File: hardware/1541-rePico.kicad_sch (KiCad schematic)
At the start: 11 parts, among them J1 Display Connector, J2 Conn_02x03_Odd_Even, J3 RESET_1541, J4 SD Card Module Connector, J5 EXT_5V, SW1 RESET, U1 Pico

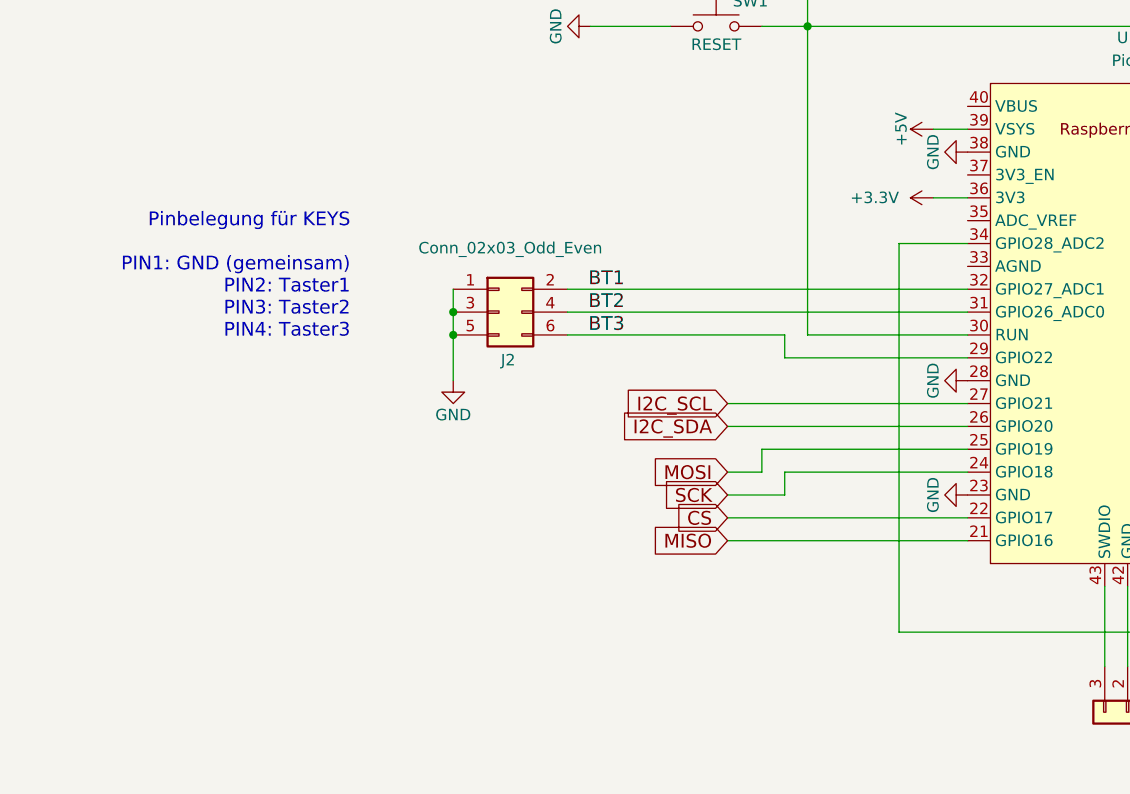
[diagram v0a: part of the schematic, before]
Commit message: new PCB layout + BRDY fix
changed rotary-encoder connector to default 5 pin
flipped BRDY signal (GPIO28) with BT3 (GPIO22) to
 not violate 5V tollerance of GPIO28.
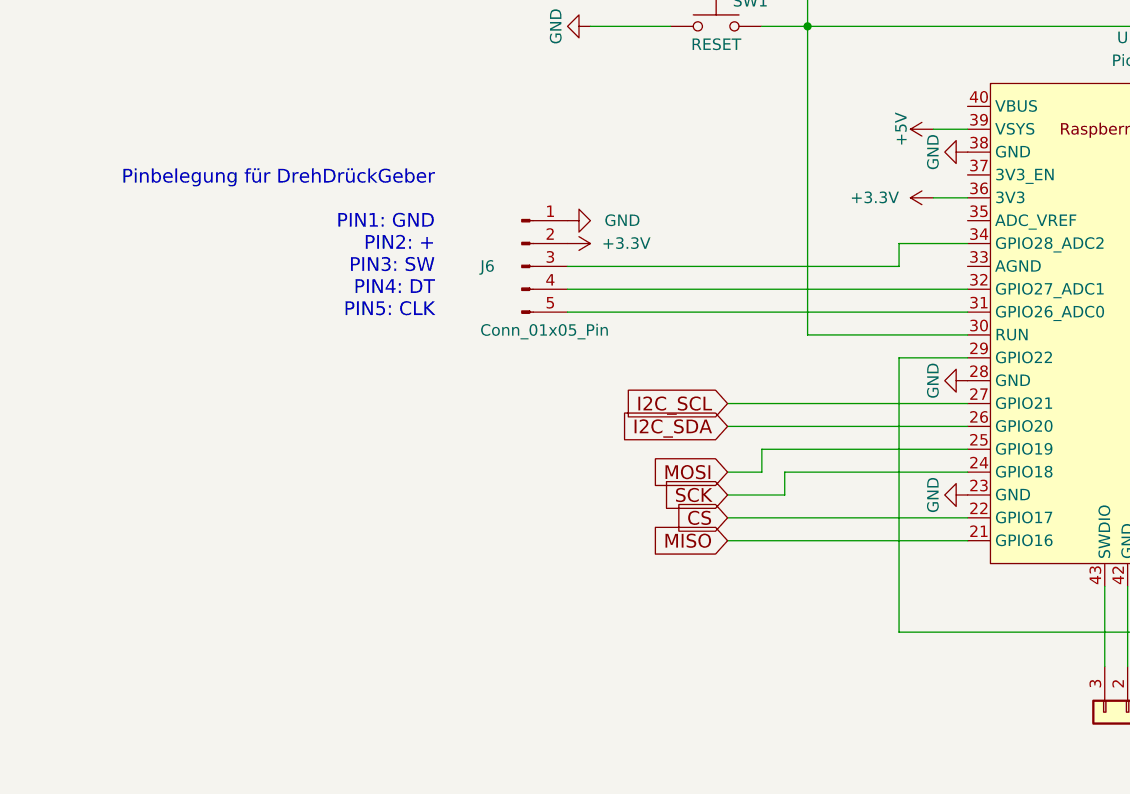
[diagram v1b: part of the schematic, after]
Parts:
- removed J2: Conn_02x03_Odd_Even, Connector_PinHeader_2.54mm:PinHeader_2x03_P2.54mm_Vertical, symbol Connector_Generic:Conn_02x03_Odd_Even
- added J6: Conn_01x05_Pin, Connector_PinHeader_2.54mm:PinHeader_1x05_P2.54mm_Vertical, symbol Connector:Conn_01x05_Pin
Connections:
- net BT3 is gone; now on net VIA 6522 Sockel/BRDY: U1.29 (GPIO22)
- net +3.3V: now also J6.2 (Pin_2)
- net GND: now also J6.1 (Pin_1)
- net VIA 6522 Sockel/BRDY: no longer U1.34 (GPIO28_ADC2)
- net BT1: no longer names the net of U1.32 (GPIO27_ADC1)
- net BT1: now also J6.4 (Pin_4)
- net BT2: no longer names the net of U1.31 (GPIO26_ADC0)
- net BT2: now also J6.5 (Pin_5)
- new net: J6.3 (Pin_3), U1.34 (GPIO28_ADC2)
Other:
- note added: "Pinbelegung für DrehDrückGeber PIN1: GND PIN2: + PIN3: SW PIN4: DT PIN5: CLK"
- note removed: "Pinbelegung für KEYS PIN1: GND (gemeinsam) PIN2: Taster1 PIN3: Taster2 PIN4: Taster3"

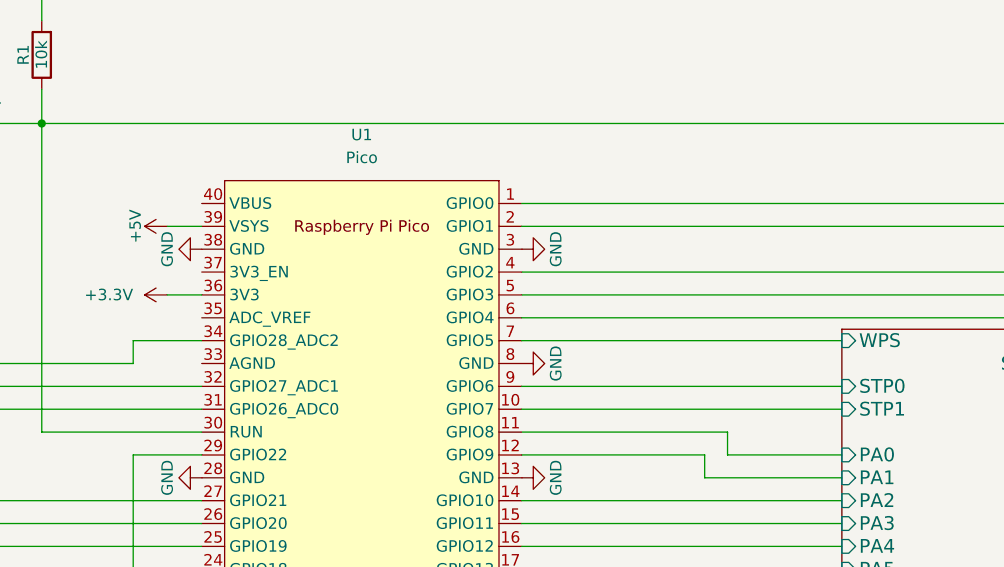
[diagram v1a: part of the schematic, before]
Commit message: new PCB layout to support WPS external
invert WPS signal to be used as input of photo-sensor
circuit of 1541-main pcb.
avoids the concurrent access of the WPS signal between
GateArray and VIA - now this comes from 74LS04
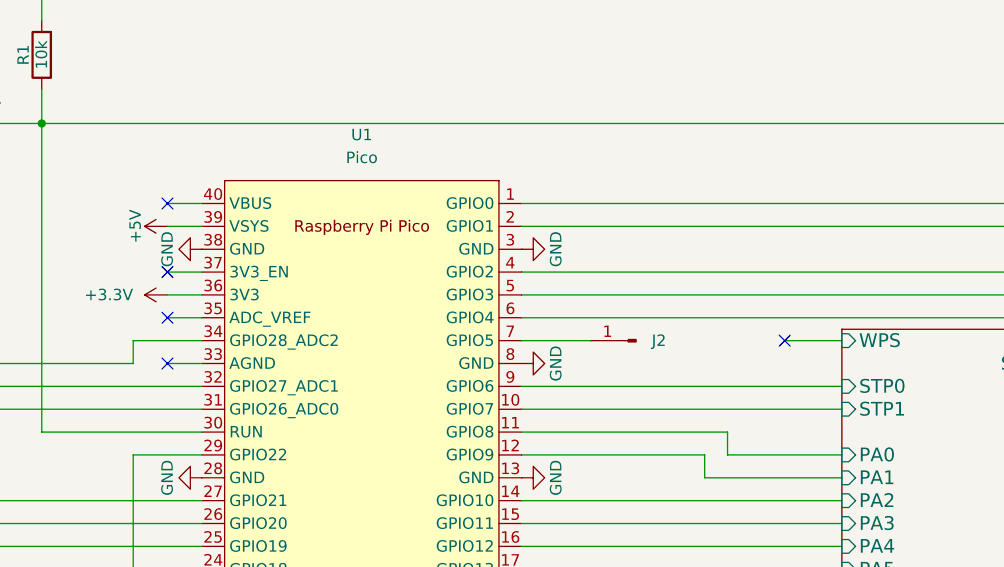
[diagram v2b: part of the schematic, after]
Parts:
- added J2: Conn_01x01_Pin, Connector_PinHeader_2.00mm:PinHeader_1x01_P2.00mm_Vertical, symbol Connector:Conn_01x01_Pin
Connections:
- net VIA 6522 Sockel/WPS: no longer U1.7 (GPIO5)
- new net: J2.1 (Pin_1), U1.7 (GPIO5)
- no-connect marks 0 -> 5
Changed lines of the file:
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@@
 		(title "1541-rePico")
 		(date "2026-02-15")
-		(rev "1.3")
+		(rev "1.4")
 	)
 	(text "Jumper Normal offen"
@@
 		(color 0 0 0 0)
 	)
+	(no_connect
+		(at 116.84 85.09)
+	)
+	(no_connect
+		(at 116.84 80.01)
+	)
+	(no_connect
+		(at 116.84 90.17)
+	)
+	(no_connect
+		(at 116.84 72.39)
+	)
+	(no_connect
+		(at 185.42 87.63)
+	)
 	(wire
 		(pts
@@
 	(wire
 		(pts
+			(xy 116.84 72.39) (xy 120.65 72.39)
+		)
+		(stroke
+			(width 0)
+			(type default)
+		)
+	)
+	(wire
+		(pts
 			(xy 113.03 87.63) (xy 113.03 90.17)
 		)
@@
 	(wire
 		(pts
+			(xy 116.84 90.17) (xy 120.65 90.17)
+		)
+		(stroke
+			(width 0)
+			(type default)
+		)
+	)
+	(wire
+		(pts
 			(xy 270.51 63.5) (xy 270.51 102.87)
 		)
@@
 	(wire
 		(pts
+			(xy 116.84 80.01) (xy 120.65 80.01)
+		)
+		(stroke
+			(width 0)
+			(type default)
+		)
+	)
+	(wire
+		(pts
 			(xy 113.03 130.81) (xy 224.79 130.81)
 		)
@@
 	(wire
 		(pts
+			(xy 116.84 85.09) (xy 120.65 85.09)
+		)
+		(stroke
+			(width 0)
+			(type default)
+		)
+	)
+	(wire
+		(pts
 			(xy 222.25 87.63) (xy 219.71 87.63)
 		)
@@
 	(wire
 		(pts
-			(xy 156.21 87.63) (xy 191.77 87.63)
+			(xy 156.21 87.63) (xy 163.83 87.63)
 		)
 		(stroke
@@
 	(wire
 		(pts
+			(xy 185.42 87.63) (xy 191.77 87.63)
+		)
+		(stroke
+			(width 0)
+			(type default)
+		)
+	)
+	(wire
+		(pts
 			(xy 128.27 172.72) (xy 119.38 172.72)
 		)
@@
 					(unit 1)
 				)
+			)
+		)
+	)
+	(symbol
+		(lib_id "Connector:Conn_01x01_Pin")
+		(at 168.91 87.63 180)
+		(unit 1)
+		(exclude_from_sim no)
+		(in_bom yes)
+		(on_board yes)
+		(dnp no)
+		(property "Reference" "J2"
+			(at 171.45 87.63 0)
+			(effects
+				(font
+					(size 1.27 1.27)
+				)
+			)
+		)
+		(property "Value" "Conn_01x01_Pin"
+			(at 171.196 89.662 0)
+			(effects
+				(font
+					(size 1.27 1.27)
+				)
+				(hide yes)
+			)
+		)
+		(property "Footprint" "Connector_PinHeader_2.00mm:PinHeader_1x01_P2.00mm_Vertical"
+			(at 168.91 87.63 0)
+			(effects
+				(font
+					(size 1.27 1.27)
+				)
+				(hide yes)
+			)
+		)
+		(property "Datasheet" "~"
+			(at 168.91 87.63 0)
+			(effects
+				(font
+					(size 1.27 1.27)
+				)
+				(hide yes)
+			)
+		)
+		(property "Description" "Generic connector, single row, 01x01, script generated"
+			(at 168.91 87.63 0)
+			(effects
+				(font
+					(size 1.27 1.27)
+				)
+				(hide yes)
+			)
+		)
+		(pin "1"
+		)
+		(instances
+			(project ""
+				(path "/7c37ffbe-d8d1-4c30-ad42-fd3ef959e14d"
+					(reference "J2")
+					(unit 1)
+				)

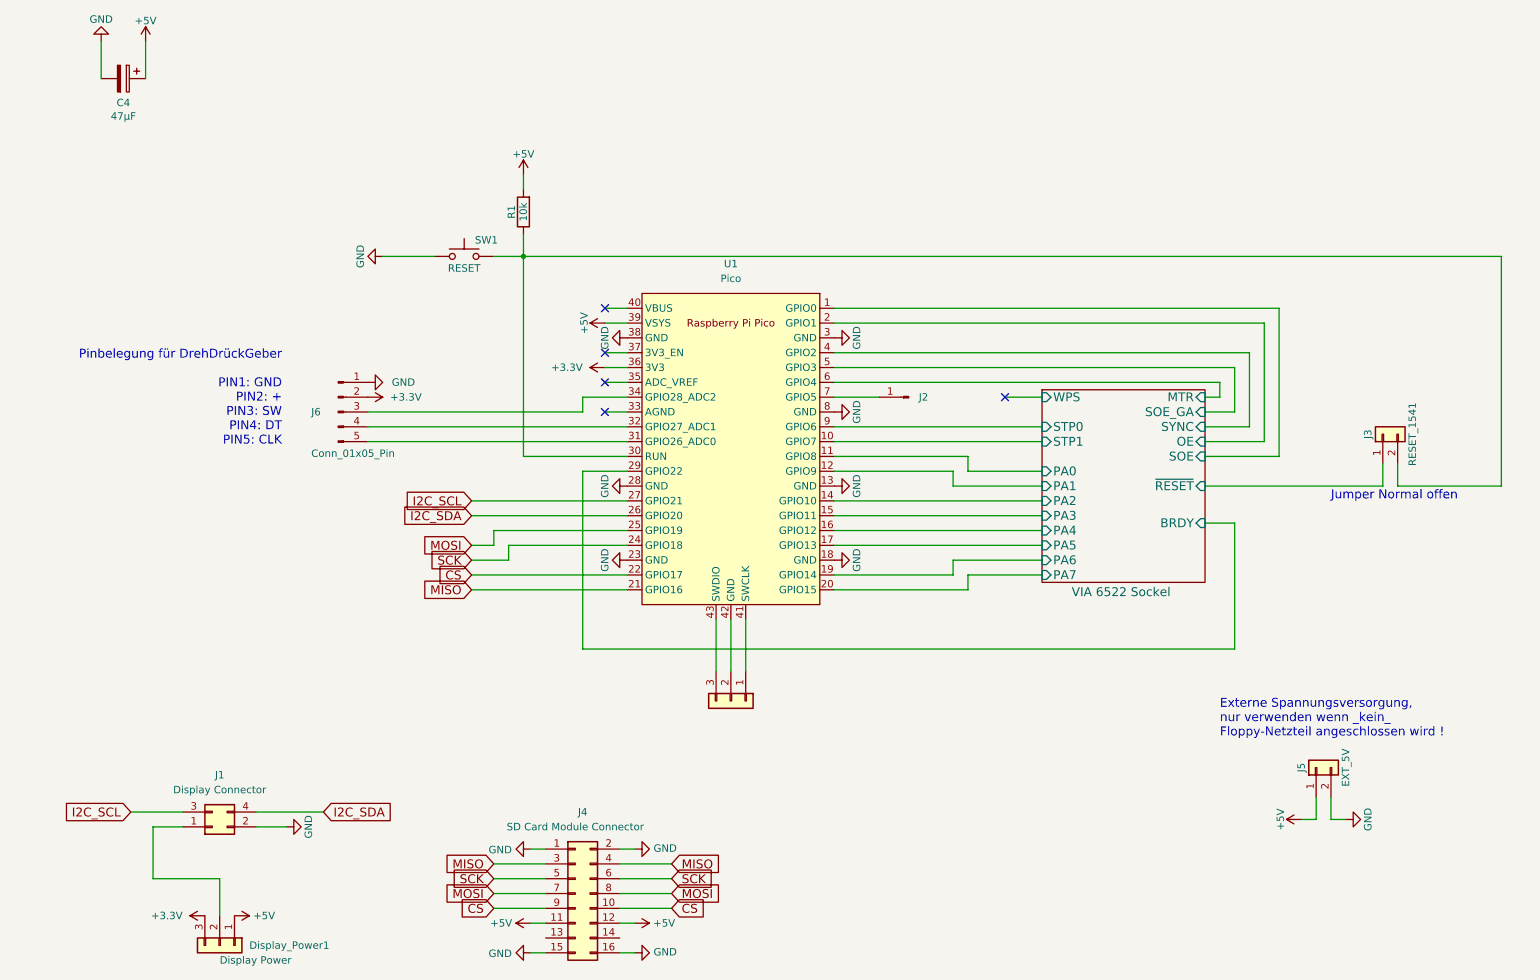
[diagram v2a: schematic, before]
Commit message: new PCB version 1.5
- added levelshifter ics txs0108epwr between pico and via pins
- added pullup-resistors for I2C (populate if necessary)
- aligned footprint of jumper-headers on 50mil grid
- added version-text and URL on backside
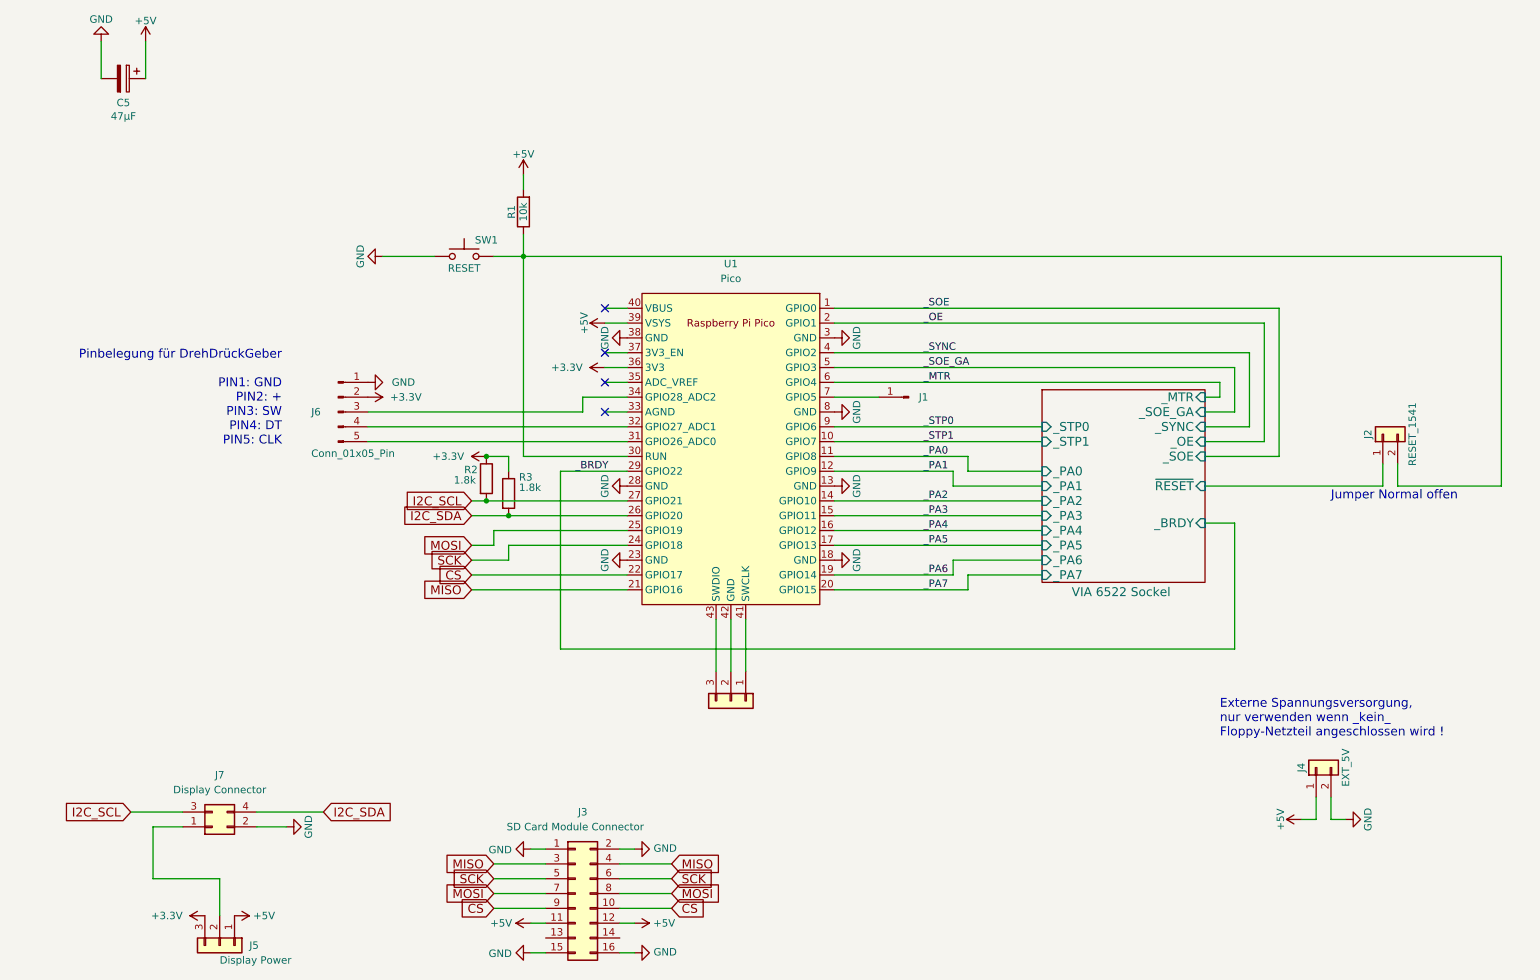
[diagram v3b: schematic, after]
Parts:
- added R2, R3: 1.8k, Resistor_SMD:R_0805_2012Metric, symbol Device:R
- renumbered C4 to C5, J2 to J1, J3 to J2, J4 to J3, J5 to J4, Display_Power1 to J5, J1 to J7
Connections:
- net +3.3V: now also R2.1, R3.1
- net I2C_SCL: now also R2.2
- net I2C_SDA: now also R3.2
- net VIA 6522 Sockel/BRDY renamed _BRDY
- net VIA 6522 Sockel/MTR renamed _MTR
- net VIA 6522 Sockel/OE renamed _OE
- net VIA 6522 Sockel/PA0 renamed _PA0
- net VIA 6522 Sockel/PA1 renamed _PA1
- net VIA 6522 Sockel/PA2 renamed _PA2
- net VIA 6522 Sockel/PA3 renamed _PA3
- net VIA 6522 Sockel/PA4 renamed _PA4
- net VIA 6522 Sockel/PA5 renamed _PA5
- net VIA 6522 Sockel/PA6 renamed _PA6
- net VIA 6522 Sockel/PA7 renamed _PA7
- net VIA 6522 Sockel/SOE renamed _SOE
- net VIA 6522 Sockel/SOE_GA renamed _SOE_GA
- net VIA 6522 Sockel/STP0 renamed _STP0
- net VIA 6522 Sockel/STP1 renamed _STP1
- net VIA 6522 Sockel/SYNC renamed _SYNC
- no-connect marks 5 -> 4
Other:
- sheet VIA 6522 Sockel ports: added _BRDY, _MTR, _OE, _PA0, _PA1, _PA2, _PA3, _PA4, _PA5, _PA6, _PA7, _SOE, _SOE_GA, _STP0, _STP1, _SYNC; removed BRDY, MTR, OE, PA0, PA1, PA2, PA3, PA4, PA5, PA6, PA7, SOE, SOE_GA, STP0, STP1, SYNC, WPS

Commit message: PCB version 1.6
- use of SN74LVC4245A for levelshifting of PortB-Signals
-> needed an inverted Mode/OE signal for DIR (done via BSS138)
- use of BSS138 for shifting of basic signals (MTR, STP,...)
- cut off "mode/OE" pin from Gatearray -> tied to GND to not let it drive PortB
- rerouted the PCB again -> alignment of Pinheaders and vias
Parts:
- renumbered C5 to C1, J7 to J1, J5 to J2, J6 to J3, J3 to J4, J1 to J5, J4 to J6, J2 to J7, R2 to R1, R3 to R2, R1 to R3
